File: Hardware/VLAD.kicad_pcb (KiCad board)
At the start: 2 copper layers, 90 x 80 mm, 100 parts, among them J1 BMP388, J2 BNO055, J3 Micro_SD_Card, J4 Conn_01x02_Male, J5 Conn_01x03_Male, J6 Conn_01x02_Male, P1 USB_C_Plug_USB2.0, Q1 S8050, Q2 S8050, Q3 S8550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

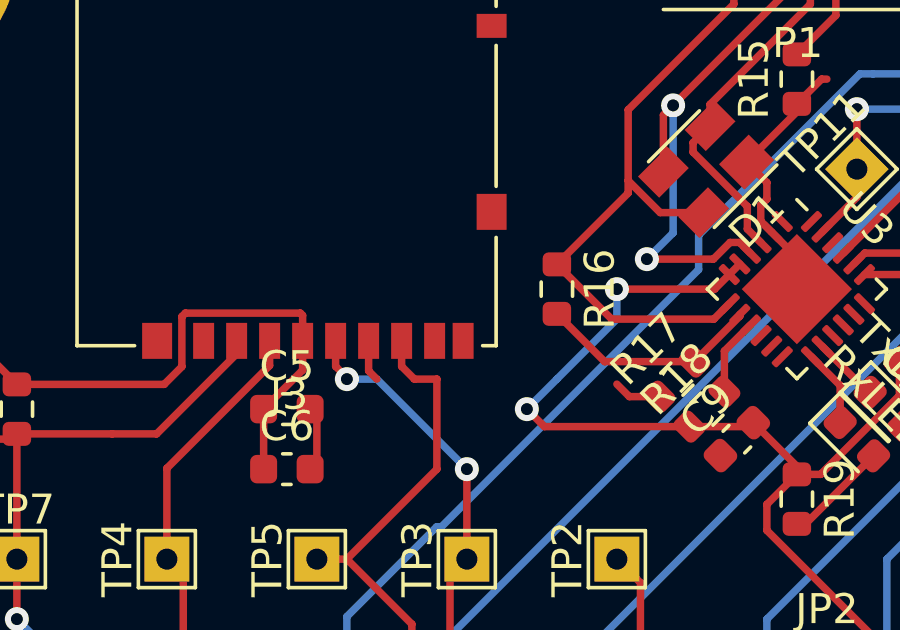
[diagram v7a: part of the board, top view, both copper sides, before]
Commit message: Re-did some no-fill zones
For SD card
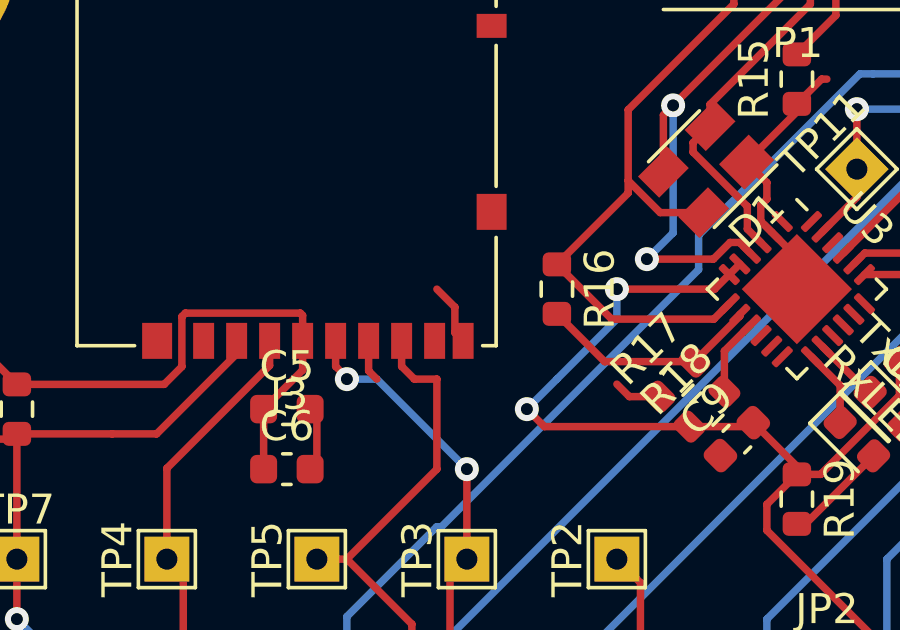
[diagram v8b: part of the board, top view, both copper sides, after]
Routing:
- net GND: track 26.3 -> 28.4 mm
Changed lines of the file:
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@@
     (thickness 1.6)
     (drawings 4)
-    (tracks 546)
+    (tracks 549)
     (zones 0)
     (modules 100)
@@
     (38 B.Mask user)
     (39 F.Mask user)
-    (40 Dwgs.User user hide)
+    (40 Dwgs.User user)
     (41 Cmts.User user)
     (42 Eco1.User user)
@@
   (segment (start 53.444431 55.919431) (end 53.808197 55.919431) (width 0.25) (layer F.Cu) (net 1))
   (segment (start 53 55.475) (end 53.444431 55.919431) (width 0.25) (layer F.Cu) (net 1))
-  (segment (start 40.725 37.725) (end 40.725 38.725) (width 0.25) (layer F.Cu) (net 1))
-  (segment (start 40.725 38.725) (end 41 39) (width 0.25) (layer F.Cu) (net 1))
   (segment (start 55 29.825) (end 55.825 29) (width 0.25) (layer F.Cu) (net 1))
   (segment (start 55.825 29) (end 56 29) (width 0.25) (layer F.Cu) (net 1))
@@
   (segment (start 50.416637 39.583363) (end 49.416637 39.583363) (width 0.25) (layer F.Cu) (net 1))
   (segment (start 49.416637 39.583363) (end 49 39.166726) (width 0.25) (layer F.Cu) (net 1))
+  (segment (start 40.725 37.725) (end 40.725 38.725) (width 0.25) (layer F.Cu) (net 1))
+  (segment (start 40.725 38.725) (end 41 39) (width 0.25) (layer F.Cu) (net 1))
+  (segment (start 43.600001 37.450001) (end 43.600001 36.600001) (width 0.25) (layer F.Cu) (net 1))
+  (segment (start 43.875 37.725) (end 43.600001 37.450001) (width 0.25) (layer F.Cu) (net 1))
+  (segment (start 43.600001 36.600001) (end 43 36) (width 0.25) (layer F.Cu) (net 1))
   (segment (start 93.775 47.775) (end 93.62 47.62) (width 1) (layer F.Cu) (net 2))
   (segment (start 96 47.775) (end 93.775 47.775) (width 1) (layer F.Cu) (net 2))
@@
       )
     )
+  )
+  (zone (net 0) (net_name "") (layers F&B.Cu) (hatch edge 0.508)
+    (connect_pads (clearance 0.508))
+    (min_thickness 0.254)
+    (keepout (tracks not_allowed) (vias not_allowed) (copperpour allowed))
+    (fill (arc_segments 32) (thermal_gap 0.508) (thermal_bridge_width 0.508))
+    (polygon
+      (pts
+        (xy 32 21) (xy 36 21) (xy 36 24) (xy 32 24)
+      )
+    )
+  )
+  (zone (net 0) (net_name "") (layers F&B.Cu) (hatch edge 0.508)
+    (connect_pads (clearance 0.508))
+    (min_thickness 0.254)
+    (keepout (tracks not_allowed) (vias not_allowed) (copperpour not_allowed))
+    (fill (arc_segments 32) (thermal_gap 0.508) (thermal_bridge_width 0.508))
+    (polygon
+      (pts
+        (xy 34 31) (xy 43 31) (xy 43 23) (xy 46 23) (xy 46 37)
+        (xy 46 38) (xy 44 37) (xy 44 33) (xy 34 33)
+      )
+    )
